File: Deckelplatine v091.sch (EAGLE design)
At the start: 67 parts, among them IC1 MAX1487EESA+, IC2 74HCT595D, IC3 74HCT595D, IC4 74HCT595D, IC5 74HCT595D, IC6 74HCT595D, J1 52808-2570, Q1 BC846BSMD, Q2 BC846BSMD, U1 LM2676S, X1 236-406/000-023, X2 233-502

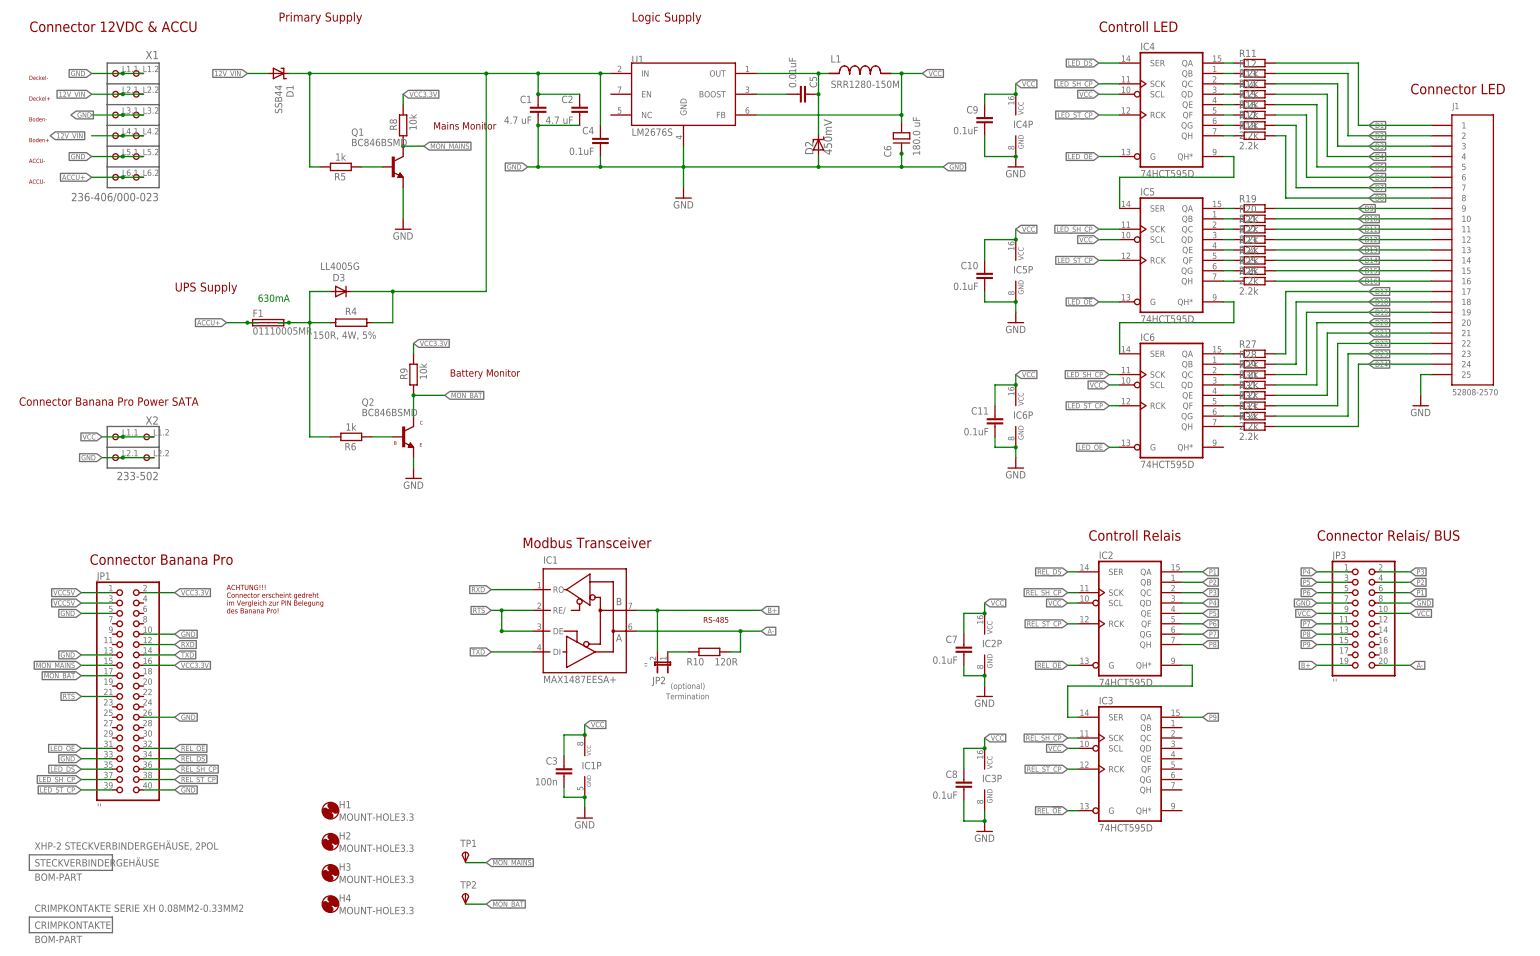
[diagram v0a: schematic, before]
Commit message: Begin mit dem Bord der Bodenplatine
Schriften in den Schaltplänen einheitlich gemacht (Layer und Große)
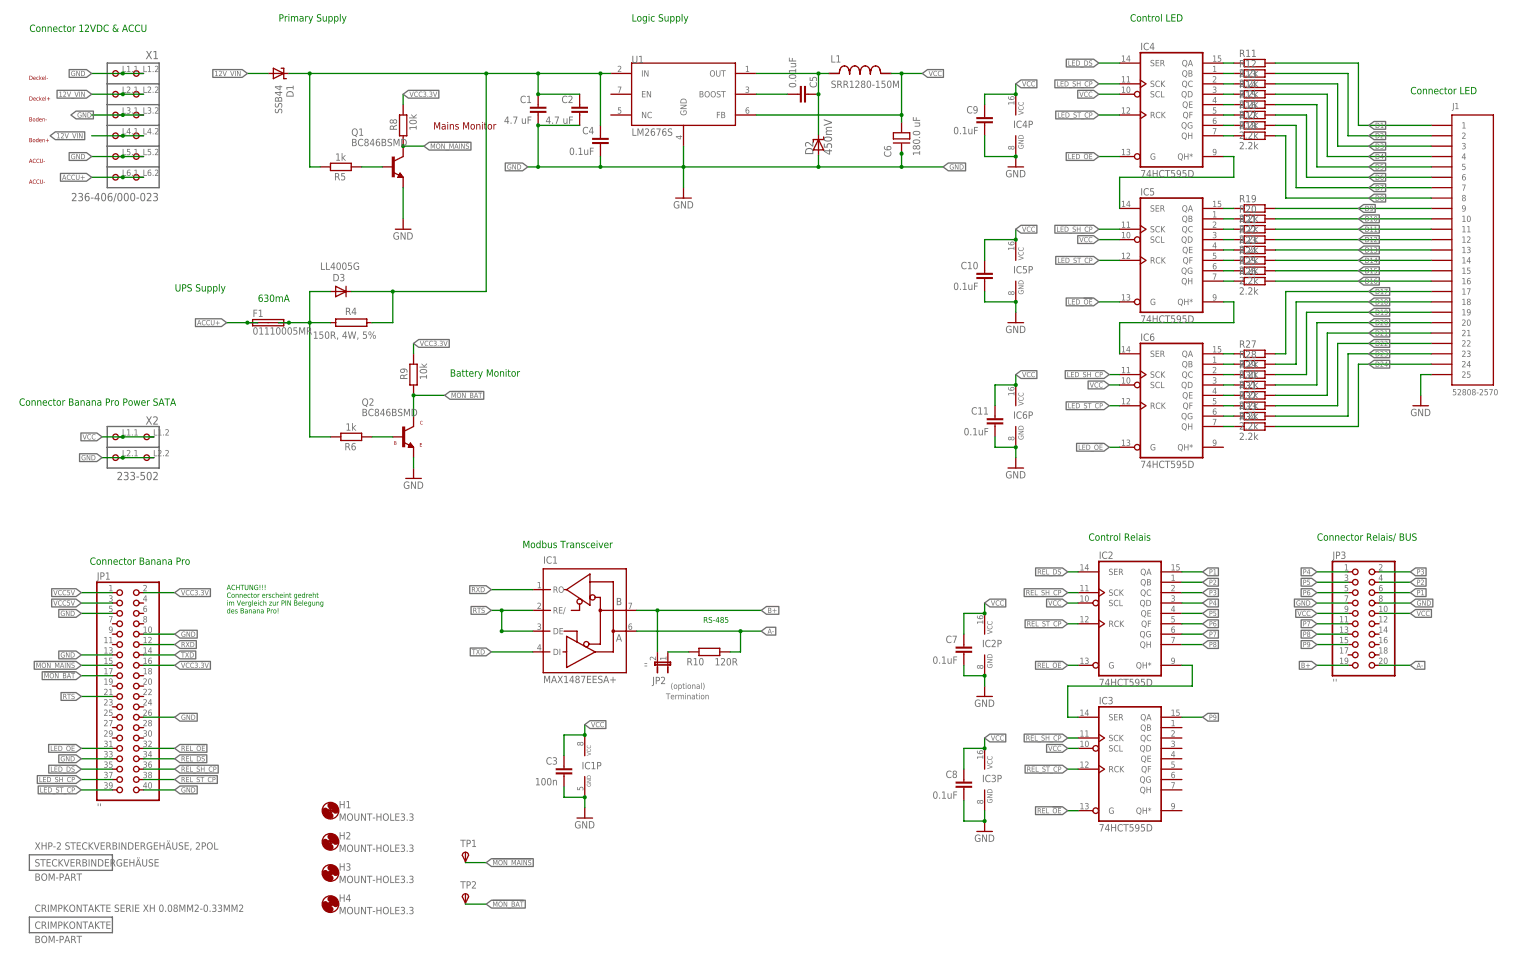
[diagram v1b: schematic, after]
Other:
- note added: "Control LED"
- note added: "Control Relais"
- note removed: "Controll LED"
- note removed: "Controll Relais"
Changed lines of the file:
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@@
 <sheet>
 <plain>
-<text x="327.66" y="119.38" size="2.54" layer="94" font="vector">Connector Relais/ BUS</text>
-<text x="27.4574" y="113.4872" size="2.54" layer="94" font="vector">Connector Banana Pro</text>
-<text x="177.5206" y="99.2886" size="1.4224" layer="94" ratio="12">RS-485</text>
+<text x="327.66" y="119.38" size="1.778" layer="91" font="vector">Connector Relais/ BUS</text>
+<text x="27.4574" y="113.4872" size="1.778" layer="91" font="vector">Connector Banana Pro</text>
+<text x="177.5206" y="99.2886" size="1.4224" layer="91" ratio="12">RS-485</text>
 <text x="179.0446" y="82.0166" size="1.4224" layer="95" ratio="12" rot="R180">Termination</text>
 <text x="178.0286" y="84.5566" size="1.4224" layer="95" ratio="12" rot="R180">(optional)</text>
-<text x="133.3246" y="117.5766" size="2.54" layer="94" font="vector">Modbus Transceiver</text>
-<text x="350.52" y="228.6" size="2.54" layer="94" font="vector">Connector LED</text>
-<text x="274.32" y="243.84" size="2.54" layer="94" font="vector">Controll LED</text>
-<text x="271.78" y="119.38" size="2.54" layer="94" font="vector">Controll Relais</text>
-<text x="12.7" y="243.84" size="2.54" layer="94" font="vector">Connector 12VDC &amp; ACCU</text>
-<text x="48.26" y="180.34" size="2.1844" layer="94" ratio="12">UPS Supply</text>
-<text x="115.57" y="159.512" size="1.778" layer="94" ratio="10">Battery Monitor</text>
+<text x="133.3246" y="117.5766" size="1.778" layer="91" font="vector">Modbus Transceiver</text>
+<text x="350.52" y="228.6" size="1.778" layer="91" font="vector">Connector LED</text>
+<text x="281.94" y="246.38" size="1.778" layer="91" font="vector">Control LED</text>
+<text x="271.78" y="119.38" size="1.778" layer="91" font="vector">Control Relais</text>
+<text x="12.7" y="243.84" size="1.778" layer="91" font="vector">Connector 12VDC &amp; ACCU</text>
+<text x="48.26" y="180.34" size="1.778" layer="91" ratio="12">UPS Supply</text>
+<text x="115.57" y="159.512" size="1.778" layer="91" ratio="10">Battery Monitor</text>
 <text x="111.506" y="219.964" size="1.778" layer="94" ratio="10">Mains Monitor</text>
-<text x="73.66" y="246.38" size="2.1844" layer="94" ratio="12">Primary Supply</text>
-<text x="160.02" y="246.38" size="2.1844" layer="94" ratio="12">Logic Supply</text>
-<text x="10.16" y="152.4" size="2.032" layer="94" font="vector">Connector Banana Pro Power SATA</text>
+<text x="73.66" y="246.38" size="1.778" layer="91" ratio="12">Primary Supply</text>
+<text x="160.02" y="246.38" size="1.778" layer="91">Logic Supply</text>
+<text x="10.16" y="152.4" size="1.778" layer="91" font="vector">Connector Banana Pro Power SATA</text>
 <text x="68.58" y="177.8" size="1.778" layer="91">630mA</text>
 <text x="12.5984" y="211.7852" size="1.016" layer="94" font="vector">ACCU-</text>
@@
 <text x="108.204" y="147.8026" size="0.889" layer="94">C</text>
 <text x="108.1278" y="142.3924" size="0.889" layer="94">E</text>
-<text x="60.96" y="101.6" size="1.27" layer="94">ACHTUNG!!!
+<text x="60.96" y="101.6" size="1.27" layer="91">ACHTUNG!!!
 Connector erscheint gedreht
 im Vergleich zur PIN Belegung
